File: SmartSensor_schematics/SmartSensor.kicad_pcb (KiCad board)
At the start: 2 copper layers, 70.6 x 74.4 mm, 48 parts, among them IC1 DS1337+, J1 Conn_01x01_Female, J2 Conn_01x01_Female, J3 Conn_02x04_Odd_Even, J5 USB_B_Micro, Q1 MMBF170, Q2 2N7002, Q3 2N7002, Q4 2N7002, SW1 SW_Push, U1 LTC3536EMSEPBF, U2 MCP9808_MSOP, U3 DMG2301L, X1 XTAL

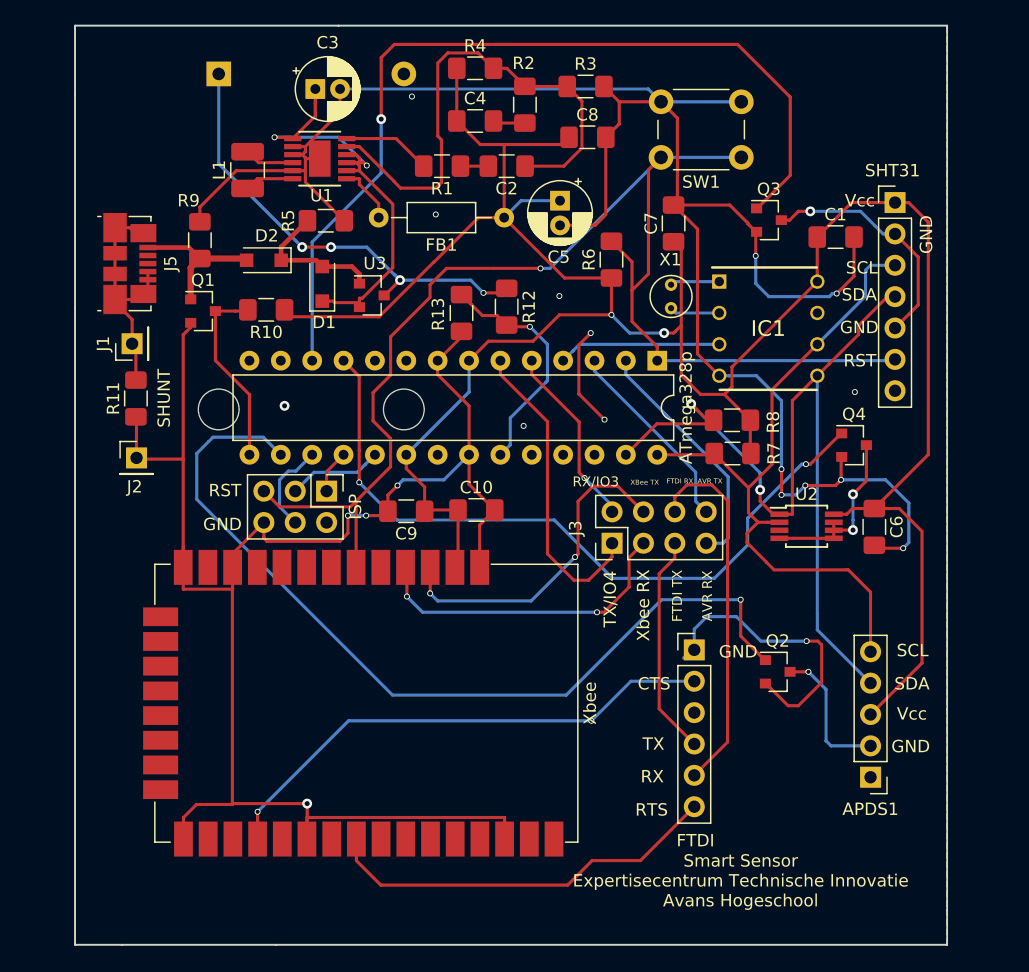
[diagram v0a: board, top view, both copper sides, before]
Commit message: delay: increment startup time
Signed-off-by: Michel Megens <dev@bietje.net>
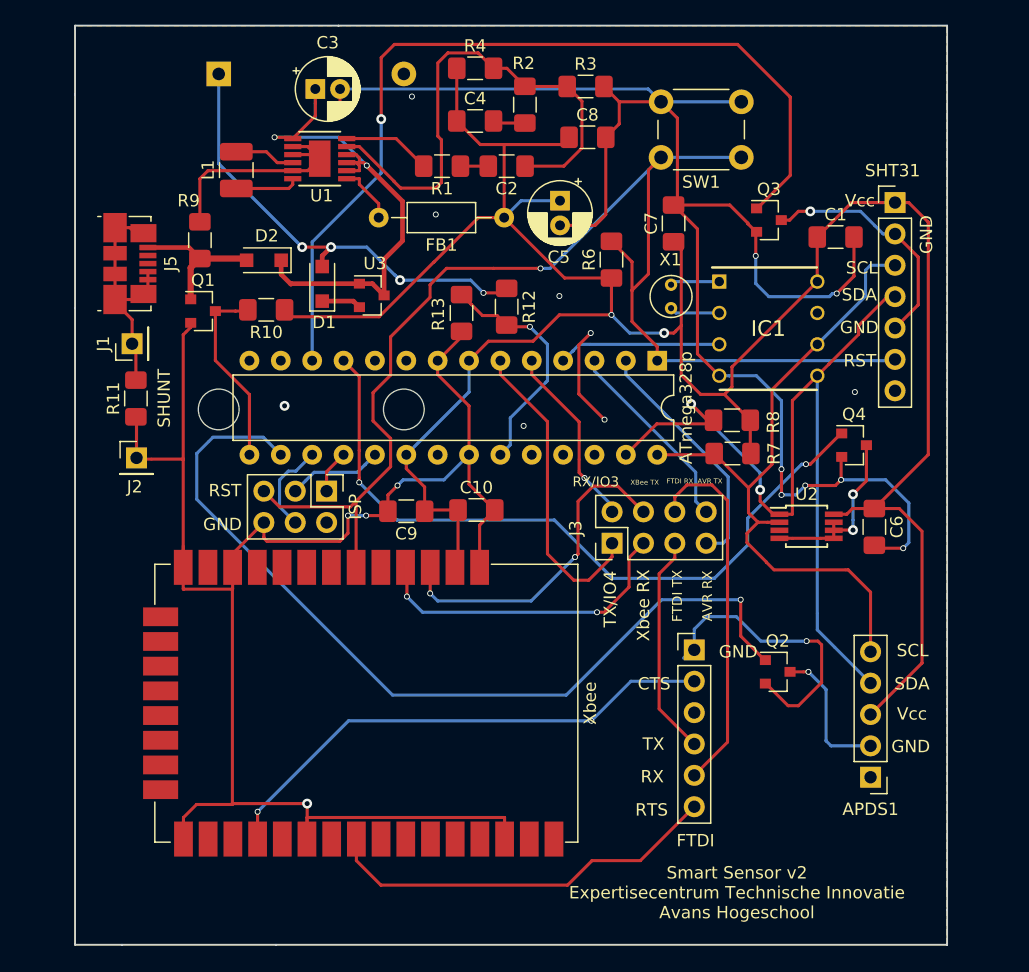
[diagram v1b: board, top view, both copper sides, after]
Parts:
- removed R5: 100kΩ, Resistor_SMD:R_1206_3216Metric_Pad1.42x1.75mm_HandSolder
- moved L1 0.91 mm to (93.3, 95.5)
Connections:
- D1 pad 1: Net-(C3-Pad1) -> Net-(D1-Pad1)
- D1 pad 2: Net-(D1-Pad2) -> +BATT
- D2 pad 1: Net-(D1-Pad2) -> Net-(C3-Pad1)
- U3 pad 1: Net-(D1-Pad2) -> Net-(C3-Pad1)
- U3 pad 2: Net-(C3-Pad1) -> Net-(D1-Pad1)
- U3 pad 3: +BATT -> Net-(C3-Pad1)
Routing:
- net Net-(D1-Pad2): track 11.7 -> 0.00 mm
- net GND: track 333.8 -> 327.6 mm
- net Net-(C3-Pad1): track 39.6 -> 45.7 mm
- net Net-(D1-Pad1): track 0.00 -> 3.21 mm
- net Net-(L1-Pad1): track 3.99 -> 5.17 mm
- net Net-(L1-Pad2): track 4.02 -> 4.94 mm
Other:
- board text added: "Smart Sensor v2 Expertisecentrum Technische Innovatie Avans Hogeschool"
- board text removed: "Smart Sensor Expertisecentrum Technische Innovatie Avans Hogeschool"

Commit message: schematics: update the schematics to v3
Update schematics to version 3.

Signed-off-by: Michel Megens <michel@michelmegens.net>
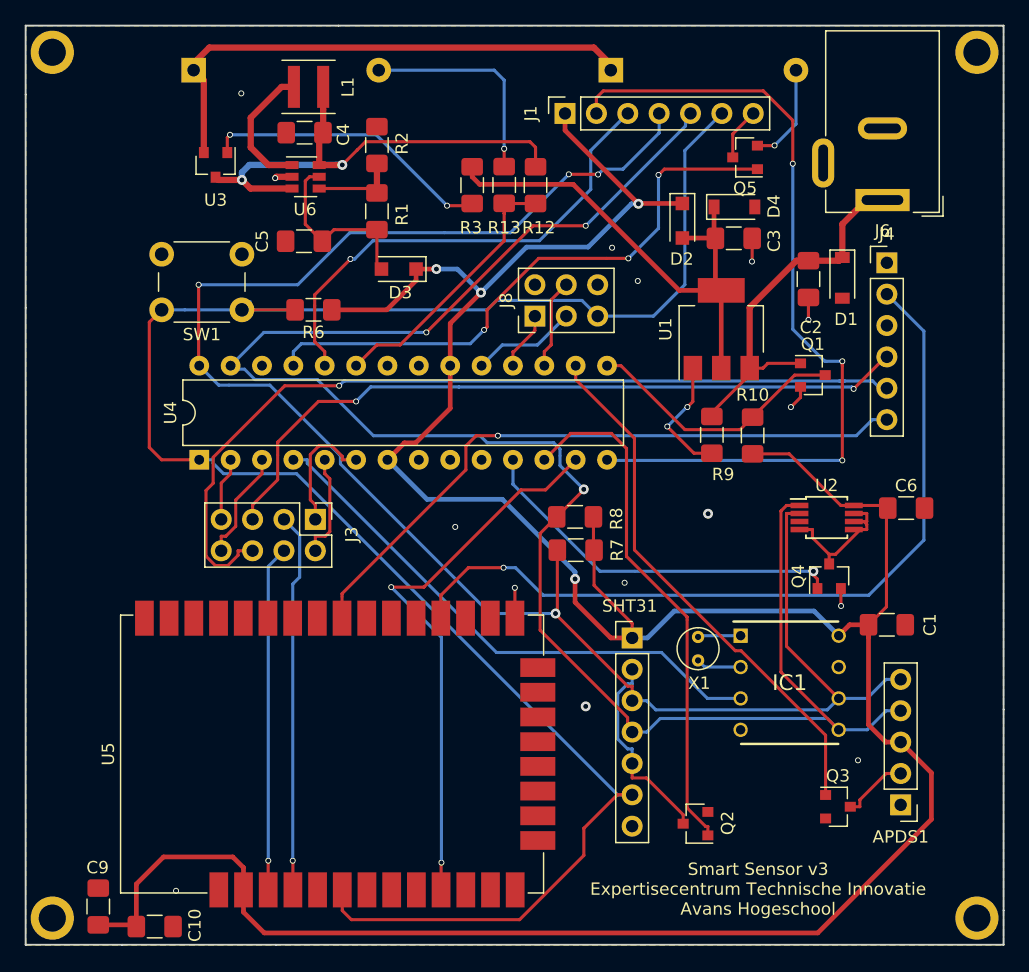
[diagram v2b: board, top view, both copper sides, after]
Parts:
- removed ATmega328p: ATmega328-PU, Package_DIP:DIP-28_W7.62mm
- removed C7: 220nF, Capacitor_SMD:C_1206_3216Metric_Pad1.42x1.75mm_HandSolder
- removed C8: 100nF, Capacitor_SMD:C_1206_3216Metric_Pad1.42x1.75mm_HandSolder
- removed FB1: BL01RN1A1F1J, Inductor_THT:L_Axial_L5.3mm_D2.2mm_P10.16mm_Horizontal_Vishay_IM-1
- removed FTDI: FTDI cable connector, Connector_PinHeader_2.54mm:PinHeader_1x06_P2.54mm_Vertical
- removed ISP: 6 PIN ISP, Connector_PinHeader_2.54mm:PinHeader_2x03_P2.54mm_Vertical
- removed J2: Conn_01x01_Female, Connector_PinHeader_2.54mm:PinHeader_1x01_P2.54mm_Vertical
- removed J5: USB_B_Micro, Connector_USB:USB_Micro-B_Molex_47346-0001
- removed R11: 25mΩ, Resistor_SMD:R_1206_3216Metric_Pad1.42x1.75mm_HandSolder
- removed R4: 1000kΩ, Resistor_SMD:R_1206_3216Metric_Pad1.42x1.75mm_HandSolder
- removed Xbee: XBee_SMT, RF_Module:Digi_XBee_SMT
- added BT2: Battery_Cell, BatteryPack:BatteryHolder_Keystone_2462_2xAA_NO_HOLES, B.Cu at (123.6, 87.4)
- added D3: MBR230, Diode_SMD:D_SOD-123F, F.Cu at (106.5, 103.5)
- added D4: 1N4148W, Diode_SMD:D_SOD-123, F.Cu at (133.7, 98.5)
- added J4: FTDI cable connector, Connector_PinHeader_2.54mm:PinHeader_1x06_P2.54mm_Vertical, F.Cu at (146.0, 103.0)
- added J6: Barrel_Jack, Connector_BarrelJack:BarrelJack_Wuerth_6941xx301002, F.Cu at (145.6, 97.9)
- added J8: 6 PIN ISP, Connector_PinHeader_2.54mm:PinHeader_2x03_P2.54mm_Vertical, F.Cu at (117.5, 107.3)
- added Q5: MMBF170, Package_TO_SOT_SMD:SOT-23, F.Cu at (134.5, 94.5)
- added REF**: MountingHole_2.2mm_M2_ISO7380_Pad, MountingHole:MountingHole_2.2mm_M2_ISO7380_Pad, F.Cu at (153.3, 86.0)
- added REF**: MountingHole_2.2mm_M2_ISO7380_Pad, MountingHole:MountingHole_2.2mm_M2_ISO7380_Pad, F.Cu at (78.4, 156.1)
- added REF**: MountingHole_2.2mm_M2_ISO7380_Pad, MountingHole:MountingHole_2.2mm_M2_ISO7380_Pad, F.Cu at (78.4, 86.0)
- added REF**: MountingHole_2.2mm_M2_ISO7380_Pad, MountingHole:MountingHole_2.2mm_M2_ISO7380_Pad, F.Cu at (153.3, 156.1)
- added U4: ATmega328-PU, Package_DIP:DIP-28_W7.62mm, F.Cu at (90.3, 119.0)
- added U5: XBee_SMT, RF_Module:Digi_XBee_SMT, F.Cu at (101.8, 142.8)
- added U6: MCP1640BCH, Package_TO_SOT_SMD:SOT-23-6, F.Cu at (98.9, 96.1)
- BT1: footprint Battery:BatteryHolder_Keystone_2462_2xAA -> BatteryPack:BatteryHolder_Keystone_2462_2xAA_NO_HOLES
- C2: value 220pF -> 1uF
- C3: value 10uF -> 1uF; footprint Capacitor_THT:CP_Radial_D5.0mm_P2.00mm -> Capacitor_SMD:C_1206_3216Metric_Pad1.42x1.75mm_HandSolder
- C4: value 47pF -> 1uF
- C5: value 47uF -> 10uF; footprint Capacitor_THT:CP_Radial_D5.0mm_P2.00mm -> Capacitor_SMD:C_1206_3216Metric_Pad1.42x1.75mm_HandSolder
- D1: value MBR120 -> 1N4148W; footprint Diode_SMD:D_SOD-123F -> Diode_SMD:D_SOD-123
- D2: value MBR120 -> MBR230
- J1: value Conn_01x01_Female -> Conn_01x07_Female; footprint Connector_PinHeader_2.54mm:PinHeader_1x01_P2.54mm_Vertical -> Connector_PinSocket_2.54mm:PinSocket_1x07_P2.54mm_Vertical
- L1: footprint Inductor_SMD:L_1210_3225Metric_Pad1.42x2.65mm_HandSolder -> Inductor_SMD:L_Coilcraft_XxL4040
- Q2, Q3, Q4: value 2N7002 -> MMBF170
- R1: value 49.9kΩ -> 976kΩ
- R2: value 6.49kΩ -> 562kΩ
- R3: value 221kΩ -> 4.7kΩ
- U1: value LTC3536EMSEPBF -> AZ1117-3.3; footprint LTC3536EMSEPBF:MSOP-12_MSE -> Package_TO_SOT_SMD:SOT-223-3_TabPin2
- U3: value DMG2301L -> DMG2301l
- moved Q1 49.6 mm to (140.0, 112.1)
- moved Q3 47.8 mm to (142.0, 147.1)
- moved R9 44.3 mm to (131.8, 117.0), turned to 270 degrees
- moved C10 42.6 mm to (86.7, 156.8)
- moved SW1 42.3 mm to (93.8, 106.8)
- moved D1 42.1 mm to (142.4, 104.2), turned to 270 degrees
- moved SHT31 41.2 mm to (125.4, 133.4)
- moved R10 40.7 mm to (135.1, 117.0), turned to 90 degrees
- moved C9 40.6 mm to (82.1, 155.1), turned to 90 degrees
- moved J1 39.7 mm to (119.9, 90.9)
- moved C3 36.0 mm to (133.6, 101.0)
- moved U1 35.3 mm to (132.6, 108.4), turned to 90 degrees
- moved D2 34.0 mm to (129.4, 99.6), turned to 270 degrees
- moved C1 31.7 mm to (146.0, 132.3)
- moved IC1 28.7 mm to (138.1, 137.0)
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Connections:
- APDS1 pad 3: LTC_VOUT -> +3V3
- BT1 pad 1: +BATT -> Net-(BT1-Pad1)
- C1 pad 1: LTC_VOUT -> +3V3
- C10 pad 1: LTC_VOUT -> +3V3
- C2 pad 1: Net-(C2-Pad1) -> VBUS
- C2 pad 2: Net-(C2-Pad2) -> GND
- C3 pad 1: Net-(C3-Pad1) -> LDO_out
- C4 pad 1: LTC_VOUT -> +BATT
- C4 pad 2: Net-(C4-Pad2) -> GND
- C5 pad 1: LTC_VOUT -> SMPS_out
- C6 pad 1: LTC_VOUT -> +3V3
- C9 pad 1: LTC_VOUT -> +3V3
- D1 pad 1: Net-(D1-Pad1) -> VBUS
- D1 pad 2: +BATT -> GND
- D2 pad 1: Net-(C3-Pad1) -> +3V3
- D2 pad 2: VBUS -> LDO_out
- IC1 pad 8: LTC_VOUT -> +3V3
- J1 pad 1: Net-(J1-Pad1) -> +3V3
- L1 pad 1: Net-(L1-Pad1) -> +BATT
- Q2 pad 1: APDS_IO9 -> SHT31_IO6
- Q2 pad 3: Net-(APDS1-Pad2) -> Net-(Q2-Pad3)
- Q3 pad 1: SHT31_IO6 -> APDS_IO9
- Q3 pad 3: Net-(Q3-Pad3) -> Net-(APDS1-Pad2)
- R1 pad 1: Net-(C2-Pad2) -> SMPS_out
- R10 pad 1: LTC_VOUT -> +3V3
- R2 pad 1: Net-(C4-Pad2) -> Net-(R1-Pad2)
- R2 pad 2: Net-(C2-Pad1) -> GND
- R3 pad 1: Net-(C2-Pad1) -> LDO_out
- R3 pad 2: GND -> Net-(R3-Pad2)
- R6 pad 1: LTC_VOUT -> +3V3
- R7 pad 1: LTC_VOUT -> +3V3
- R8 pad 1: LTC_VOUT -> +3V3
- SHT31 pad 1: LTC_VOUT -> +3V3
- SHT31 pad 2: Net-(Q3-Pad3) -> Net-(Q2-Pad3)
- SHT31 pad 5: Net-(Q3-Pad3) -> Net-(Q2-Pad3)
- U1 pad 1: Net-(C3-Pad1) -> GND
- U1 pad 2: GND -> LDO_out
- U1 pad 3: GND -> VBUS
- U2 pad 8: LTC_VOUT -> +3V3
- U3 pad 1: Net-(C3-Pad1) -> Net-(R3-Pad2)
- U3 pad 2: Net-(D1-Pad1) -> Net-(BT1-Pad1)
- U3 pad 3: Net-(C3-Pad1) -> +BATT
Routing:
- net GND: track 327.6 -> 46.8 mm, vias 20 -> 19
- net +3V3: track 0.00 -> 243.6 mm, vias 0 -> 4
- net LTC_VOUT: track 200.1 -> 0.00 mm, vias 2 -> 0
- net SCL: track 56.0 -> 144.4 mm, vias 0 -> 4
- net SDA: track 72.2 -> 148.3 mm, vias 2 -> 3
- net IO1: track 0.00 -> 67.8 mm, vias 0 -> 3
- net RESET: track 106.4 -> 158.6 mm, vias 1 -> 0
- net EXT_ENABLE: track 0.00 -> 48.3 mm, vias 0 -> 3
- net Net-(C3-Pad1): track 45.7 -> 0.00 mm, vias 2 -> 0
- net XB_SLEEP: track 0.00 -> 45.4 mm, vias 0 -> 2
- net Net-(BT1-Pad1): track 0.00 -> 43.0 mm
- net Net-(C2-Pad1): track 41.7 -> 0.00 mm
- net FTDI_TX: track 18.0 -> 59.4 mm, vias 0 -> 2
- net FTDI_RX: track 29.8 -> 70.9 mm, vias 0 -> 1
- net LDO_out: track 0.00 -> 40.8 mm
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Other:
- board size 70.6 x 74.4 mm -> 79.2 x 74.4 mm
- board text added: "Smart Sensor v3 Expertisecentrum Technische Innovatie Avans Hogeschool"
- board text removed: "AVR RX"
- board text removed: "AVR TX"
- board text removed: "CTS"
- board text removed: "FTDI RX"
- board text removed: "FTDI TX"
- board text removed: "GND"
- board text removed: "RST"
- board text removed: "RTS"
- board text removed: "RX"
- board text removed: "RX/IO3"
- board text removed: "SCL"
- board text removed: "SDA"
- board text removed: "SHUNT"
- board text removed: "Smart Sensor v2 Expertisecentrum Technische Innovatie Avans Hogeschool"
- board text removed: "TX"
- board text removed: "TX/IO4"
- board text removed: "Vcc"
- board text removed: "XBee TX"
- board text removed: "Xbee RX"

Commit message: schematics: implement version 3
Implement the version 3 schematics.

Signed-off-by: Michel Megens <michel@michelmegens.net>
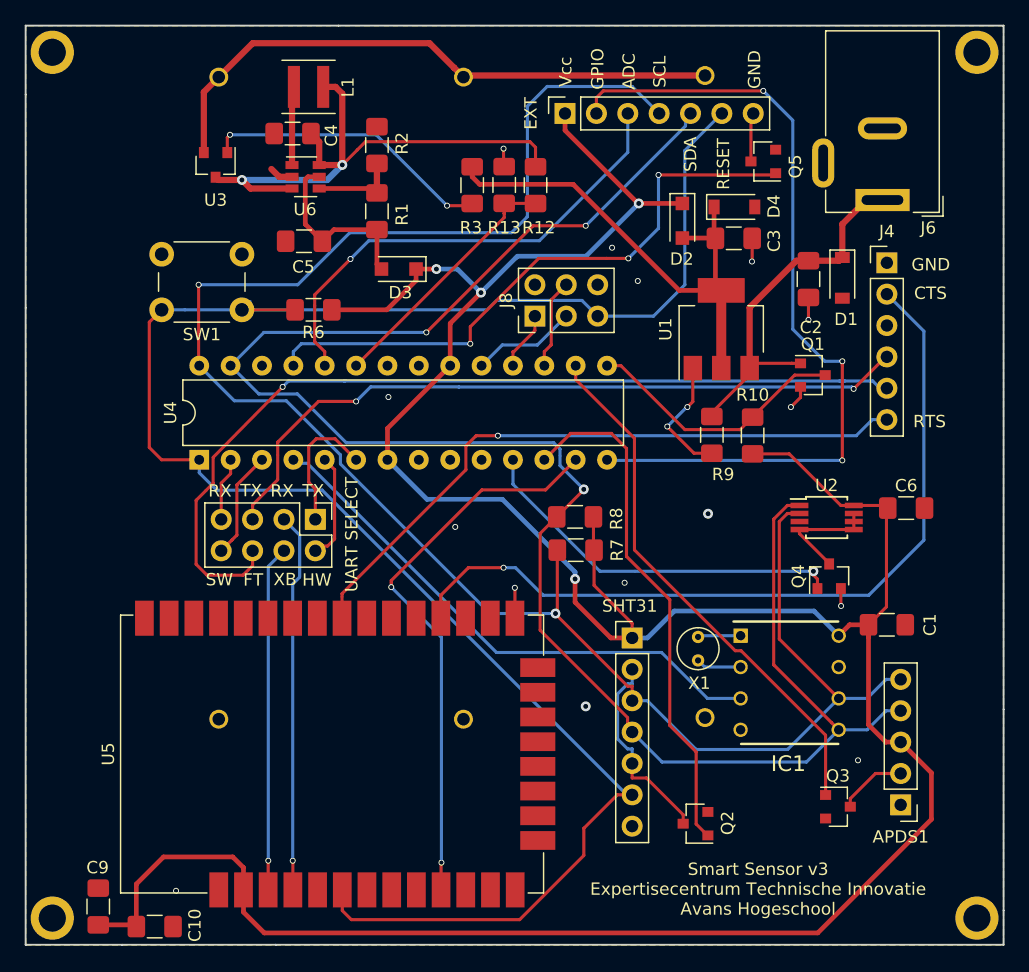
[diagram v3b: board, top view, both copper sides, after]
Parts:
- added BT3: Battery_Cell, BatteryPack:2460, B.Cu at (131.3, 113.9)
- BT1, BT2: footprint BatteryPack:BatteryHolder_Keystone_2462_2xAA_NO_HOLES -> BatteryPack:2460
- UART SELECT: renamed from J3
- moved BT2 29.1 mm to (111.8, 114.0), turned to 90 degrees
- moved BT1 26.6 mm to (91.9, 114.0), turned to 90 degrees
- moved Q5 1.51 mm to (136.0, 94.8)
- moved C4 0.98 mm to (97.9, 92.6)
- renumbered J1 to EXT
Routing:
- net GND: track 46.8 -> 23.1 mm, vias 19 -> 17
- net SCL: track 144.4 -> 153.6 mm, vias 4 -> 2
- net Net-(BT1-Pad1): track 43.0 -> 48.4 mm
- net Net-(L1-Pad2): track 10.9 -> 6.39 mm
- net SMPS_out: track 14.9 -> 17.8 mm
- net FTDI_RX: track 70.9 -> 73.7 mm
- net Net-(Q4-Pad3): track 12.3 -> 9.48 mm
- net SDA: track 148.3 -> 150.4 mm
- net EXT_ENABLE: track 48.3 -> 49.6 mm
- net +BATT: track 44.5 -> 45.7 mm
- net VBATT_ADC0: track 21.8 -> 20.7 mm
- net AVR_TX: track 10.0 -> 10.9 mm
- net VBUS: track 30.5 -> 31.1 mm
- net Net-(R1-Pad2): track 7.21 -> 7.71 mm
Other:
- board text added: "ADC"
- board text added: "CTS"
- board text added: "FT"
- board text added: "GND"
- board text added: "GPIO"
- board text added: "HW"
- board text added: "RESET"
- board text added: "RTS"
- board text added: "RX"
- board text added: "SCL"
- board text added: "SDA"
- board text added: "SW"
- board text added: "TX"
- board text added: "Vcc"
- board text added: "XB"

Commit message: schematics: implement smart sensor v4
Implement version 4 in hardware.

Signed-off-by: Michel Megens <michel@michelmegens.net>
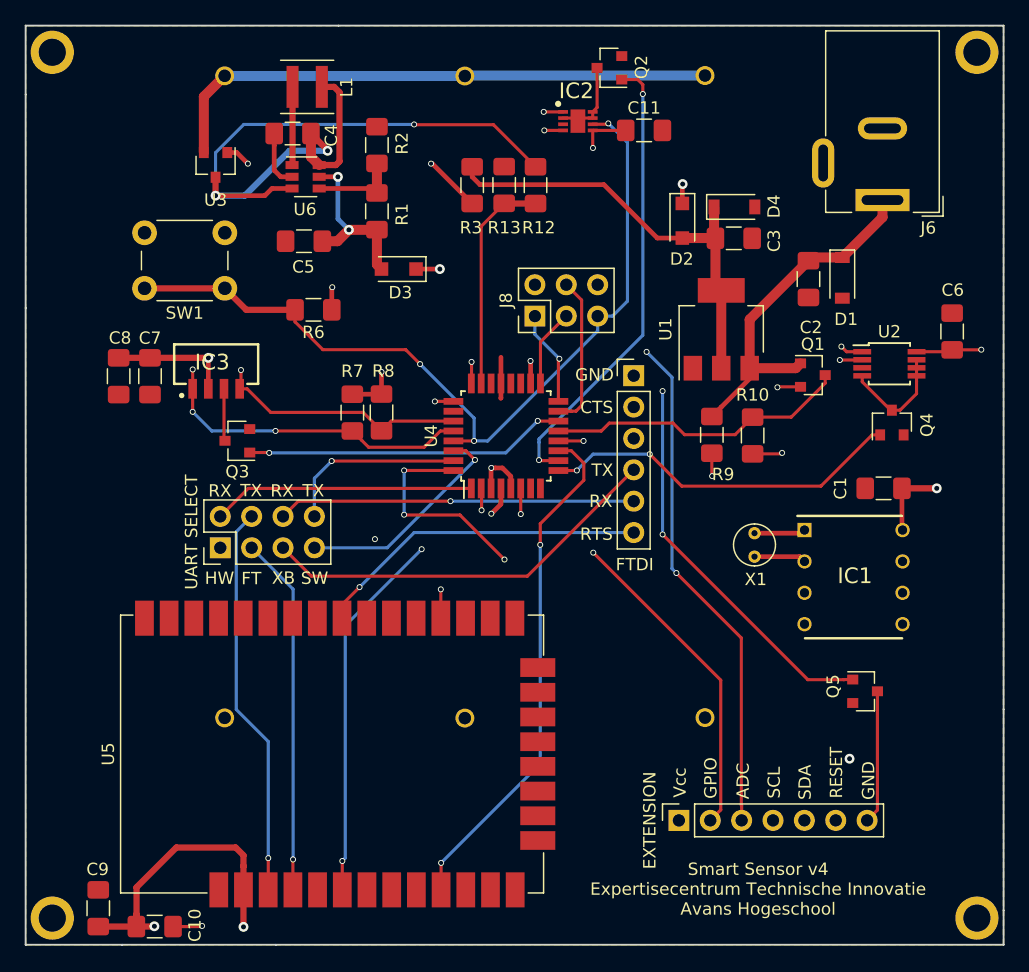
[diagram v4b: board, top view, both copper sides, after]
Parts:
- removed APDS1: APDS, Connector_PinHeader_2.54mm:PinHeader_1x05_P2.54mm_Vertical
- removed EXT: Conn_01x07_Female, Connector_PinSocket_2.54mm:PinSocket_1x07_P2.54mm_Vertical
- removed SHT31: SHT31, Connector_PinHeader_2.54mm:PinHeader_1x07_P2.54mm_Vertical
- added C11: 100nF, Capacitor_SMD:C_1206_3216Metric_Pad1.42x1.75mm_HandSolder, F.Cu at (126.3, 92.3)
- added C7: 1uF, Capacitor_SMD:C_1206_3216Metric_Pad1.42x1.75mm_HandSolder, F.Cu at (86.3, 112.2)
- added C8: 100nF, Capacitor_SMD:C_1206_3216Metric_Pad1.42x1.75mm_HandSolder, F.Cu at (83.8, 112.2)
- added EXTENSION: ÉXTENSION HEADER, Connector_PinSocket_2.54mm:PinSocket_1x07_P2.54mm_Vertical, F.Cu at (129.2, 148.2)
- added IC2: SHT31-DIS-B, SHT31-DIS-B:SON50P250X250X90-9N-D, F.Cu at (121.0, 91.6)
- added IC3: VEML7700-TT, VEML7700:VEML7700, F.Cu at (88.3, 112.8)
- U4: value ATmega328-PU -> ATmega328P-AU; footprint Package_DIP:DIP-28_W7.62mm -> Package_QFP:TQFP-32_7x7mm_P0.8mm
- moved Q2 61.6 mm to (123.5, 87.2)
- moved Q3 56.9 mm to (93.4, 117.4), turned to 180 degrees
- moved Q5 43.7 mm to (144.2, 137.7), turned to 0 degrees
- moved U4 24.9 mm to (115.2, 117.0)
- moved FTDI 22.4 mm to (125.5, 112.2)
- moved R7 21.2 mm to (102.7, 115.2), turned to 270 degrees
- moved R8 17.8 mm to (105.1, 115.1), turned to 270 degrees
- moved C6 14.8 mm to (151.3, 108.6), turned to 90 degrees
- moved Q4 13.4 mm to (146.4, 116.0)
- moved U2 13.4 mm to (146.2, 111.2)
- moved C1 11.1 mm to (145.7, 121.3), turned to 180 degrees
- moved IC1 10.00 mm to (143.3, 128.5)
- moved X1 9.56 mm to (135.3, 124.9)
- moved UART SELECT 8.03 mm to (92.0, 126.1), turned to 90 degrees
- moved SW1 2.22 mm to (92.4, 105.1)
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- renumbered J4 to FTDI, REF** to REF1, REF** to REF2, REF** to REF3, REF** to REF4
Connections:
- U4 pad 1: RESET -> AVR_RX
- U4 pad 10: Net-(U4-Pad10) -> SHT31_IO6
- U4 pad 11: TMP_IO5 -> XB_SLEEP
- U4 pad 12: SHT31_IO6 -> IO1
- U4 pad 13: XB_SLEEP -> Vadap_IO9
- U4 pad 14: IO1 -> APDS_IO9
- U4 pad 15: Vadap_IO9 -> MOSI
- U4 pad 16: APDS_IO9 -> MISO
- U4 pad 17: MOSI -> SCK
- U4 pad 18: MISO -> +3V3
- U4 pad 19: SCK -> Net-(U4-Pad19)
- U4 pad 2: AVR_DBG_RX -> AVR_TX
- U4 pad 20: +3V3 -> Net-(U4-Pad20)
- U4 pad 21: Net-(U4-Pad21) -> GND
- U4 pad 22: GND -> Net-(U4-Pad22)
- U4 pad 3: AVR_DBG_TX -> GND
- U4 pad 4: INTA_IO2 -> +3V3
- U4 pad 5: AVR_RX -> GND
- U4 pad 6: AVR_TX -> +3V3
- U4 pad 7: +3V3 -> Net-(U4-Pad7)
- U4 pad 8: GND -> Net-(U4-Pad8)
- U4 pad 9: Net-(U4-Pad9) -> TMP_IO5
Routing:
- net +3V3: track 243.1 -> 67.4 mm, vias 4 -> 14
- net FTDI_RX: track 73.7 -> 28.9 mm
- net XBEE_CTS: track 65.8 -> 28.0 mm
- net IO1: track 67.8 -> 37.7 mm, vias 3 -> 2
- net FTDI_TX: track 59.4 -> 32.9 mm, vias 2 -> 0
- net XBEE_RTS: track 53.1 -> 27.1 mm
- net +BATT: track 45.7 -> 64.0 mm, vias 2 -> 3
- net ADC1: track 39.4 -> 57.6 mm, vias 1 -> 3
- net APDS_IO9: track 43.4 -> 26.1 mm, vias 0 -> 2
- net AVR_TX: track 10.9 -> 26.8 mm, vias 0 -> 1
- net SDA: track 150.4 -> 134.9 mm
- net AVR_DBG_RX: track 5.14 -> 18.0 mm, vias 0 -> 1
- net AVR_RX: track 8.70 -> 21.3 mm
- net SCL: track 153.6 -> 142.0 mm, vias 2 -> 5
- net Net-(IC2-Pad2): track 16.3 -> 6.82 mm
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- added copper zone on PWR.Cu, net +3V3
- added copper zone on Util.Cu, net GND
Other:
- copper layers 2 -> 4
- board text added: "Smart Sensor v4 Expertisecentrum Technische Innovatie Avans Hogeschool"
- board text removed: "Smart Sensor v3 Expertisecentrum Technische Innovatie Avans Hogeschool"
